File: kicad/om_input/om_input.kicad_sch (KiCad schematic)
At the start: 55 parts, among them J1 XLR3_AudioJack3_Combo_Switch, Q1 PNP, Q2 PNP, SW1 SW_DPDT_x2, SW2 SW_4PDT_x4, U1 Opamp_Quad, U2 Opamp_Quad

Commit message: improved circuit
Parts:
- removed R22, R24: 1k5, symbol Device:R_US
- added C14: 47nF, symbol Device:C
- added C15: 100pF, symbol Device:C
- added J2: Conn_01x07_Pin, symbol Connector:Conn_01x07_Pin
- C12: value 680pF -> 100nF
- C8: value 12pF -> 15pF
- R18: value 4k7 -> 470
- R21: value 1k5 -> 100
- R23: value 1k5 -> 1M
- R9: value R_US -> 2k2
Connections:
- net +48V: now also J2.1 (Pin_1)
- net +5V: now also C14.1, J2.2 (Pin_2)
- net Earth: now also J2.4 (Pin_4)
- net GND: now also C14.2, C15.1, J2.3 (Pin_3)
- net MON: now also J2.7 (Pin_7)
- net SIG+: now also J2.5 (Pin_5)
- net SIG-: now also J2.6 (Pin_6)
- net T: now also SW2.5 (B)
- net TN: no longer SW2.5 (B)
- net at SW2.9 (C): now also C13.2; no longer C13.1
- net at U2.13 (-), U2.14: now also C13.1; no longer C13.2
- net at C12.2, R23.2, U2.12 (+): now also C15.2
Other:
- note added: "(simulated approx. gain) stage 1 gain: +5db to +35db stage 2 gain: -4db to +23db stage 2 unbalanced gain: -10db to +15db inst gain: 0db mic gain: +1db to +58db line gain: -4db to +23db inst gain: -10db to +15db"
- note added: "inst and line input"
- note added: "instrument input buffer and filter ref: 1. pg 354, fig. 12.5"
- note added: "padless balanced feedback mic preamp, stage 1 ref: 1. pg. 521, fig. 17.10"
- note added: "padless balanced feedback mic preamp, stage 2 ref: 1. pg. 522, fig. 17.11"
- note added: "phantom power indicator"
- note added: "phantom power switch"
- note added: "rev log pot"
- note added: "use FET op amp ideally"
- moved on the sheet: C1, C10, C12, C13, C2, C3, C4, C5, C6, C7, C8, C9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

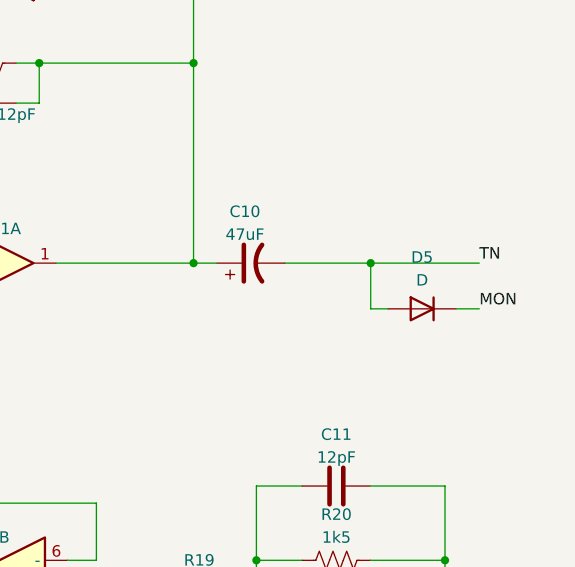
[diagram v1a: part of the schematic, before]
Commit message: removed extra mon
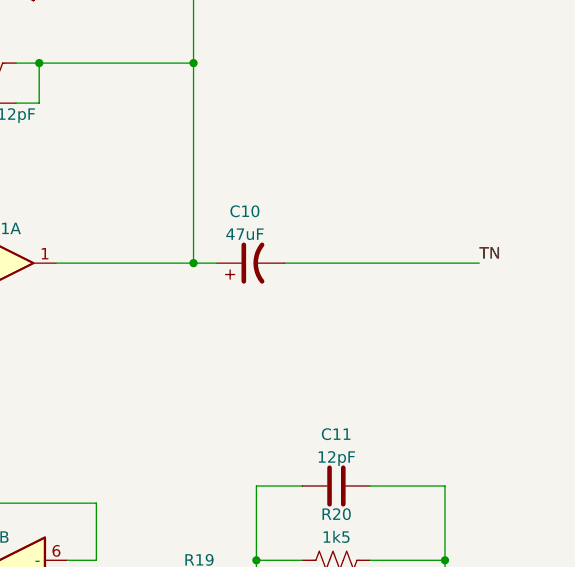
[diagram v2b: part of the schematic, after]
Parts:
- removed D5: D, symbol Device:D
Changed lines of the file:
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@@
 	)
 	(junction
-		(at 220.345 88.9)
-		(diameter 0)
-		(color 0 0 0 0)
-	)
-	(junction
 		(at 147.32 105.41)
 		(diameter 0)
@@
 	(wire
 		(pts
-			(xy 220.345 93.98) (xy 220.345 88.9)
-		)
-		(stroke
-			(width 0)
-			(type default)
-		)
-	)
-	(wire
-		(pts
 			(xy 189.865 147.32) (xy 189.865 127)
 		)
@@
 	(wire
 		(pts
-			(xy 210.82 88.9) (xy 220.345 88.9)
+			(xy 210.82 88.9) (xy 232.41 88.9)
 		)
 		(stroke
@@
 	(wire
 		(pts
-			(xy 220.345 88.9) (xy 232.41 88.9)
-		)
-		(stroke
-			(width 0)
-			(type default)
-		)
-	)
-	(wire
-		(pts
 			(xy 99.695 85.09) (xy 99.695 73.66)
 		)
@@
 	(wire
 		(pts
-			(xy 222.25 93.98) (xy 220.345 93.98)
-		)
-		(stroke
-			(width 0)
-			(type default)
-		)
-	)
-	(wire
-		(pts
-			(xy 229.87 93.98) (xy 232.41 93.98)
-		)
-		(stroke
-			(width 0)
-			(type default)
-		)
-	)
-	(wire
-		(pts
 			(xy 53.34 62.23) (xy 53.34 81.28)
 		)
@@
 		)
 	)
-	(label "MON"
-		(at 232.41 93.98 0)
-		(effects
-			(font
-				(size 1.27 1.27)
-			)
-			(justify left bottom)
-		)
-	)
 	(label "SN"
 		(at 26.67 73.66 180)
@@
 					(unit 1)
 				)
-			)
-		)
-	)
-	(symbol
-		(lib_id "Device:D")
-		(at 226.06 93.98 0)
-		(mirror y)
-		(unit 1)
-		(exclude_from_sim no)
-		(in_bom yes)
-		(on_board yes)
-		(dnp no)
-		(fields_autoplaced yes)
-		(property "Reference" "D5"
-			(at 226.06 88.265 0)
-			(effects
-				(font
-					(size 1.27 1.27)
-				)
-			)
-		)
-		(property "Value" "D"
-			(at 226.06 90.805 0)
-			(effects
-				(font
-					(size 1.27 1.27)
-				)
-			)
-		)
-		(property "Footprint" ""
-			(at 226.06 93.98 0)
-			(effects
-				(font
-					(size 1.27 1.27)
-				)
-				(hide yes)
-			)
-		)
-		(property "Datasheet" "~"
-			(at 226.06 93.98 0)
-			(effects
-				(font
-					(size 1.27 1.27)
-				)
-				(hide yes)
-			)
-		)
-		(property "Description" ""
-			(at 226.06 93.98 0)
-			(effects
-				(font
-					(size 1.27 1.27)
-				)
-			)
-		)
-		(property "Sim.Device" "D"
-			(at 226.06 93.98 0)
-			(effects
-				(font
-					(size 1.27 1.27)
-				)
-				(hide yes)
-			)
-		)
-		(property "Sim.Pins" "1=K 2=A"
-			(at 226.06 93.98 0)
-			(effects
-				(font
-					(size 1.27 1.27)
-				)
-				(hide yes)
-			)
-		)
-		(pin "1"
-		)
-		(pin "2"
-		)
-		(instances
-			(project "om_input"
-				(path "/241d8f18-f2ee-48f0-a9d7-bc33686952e8"
-					(reference "D5")
-					(unit 1)
-				)

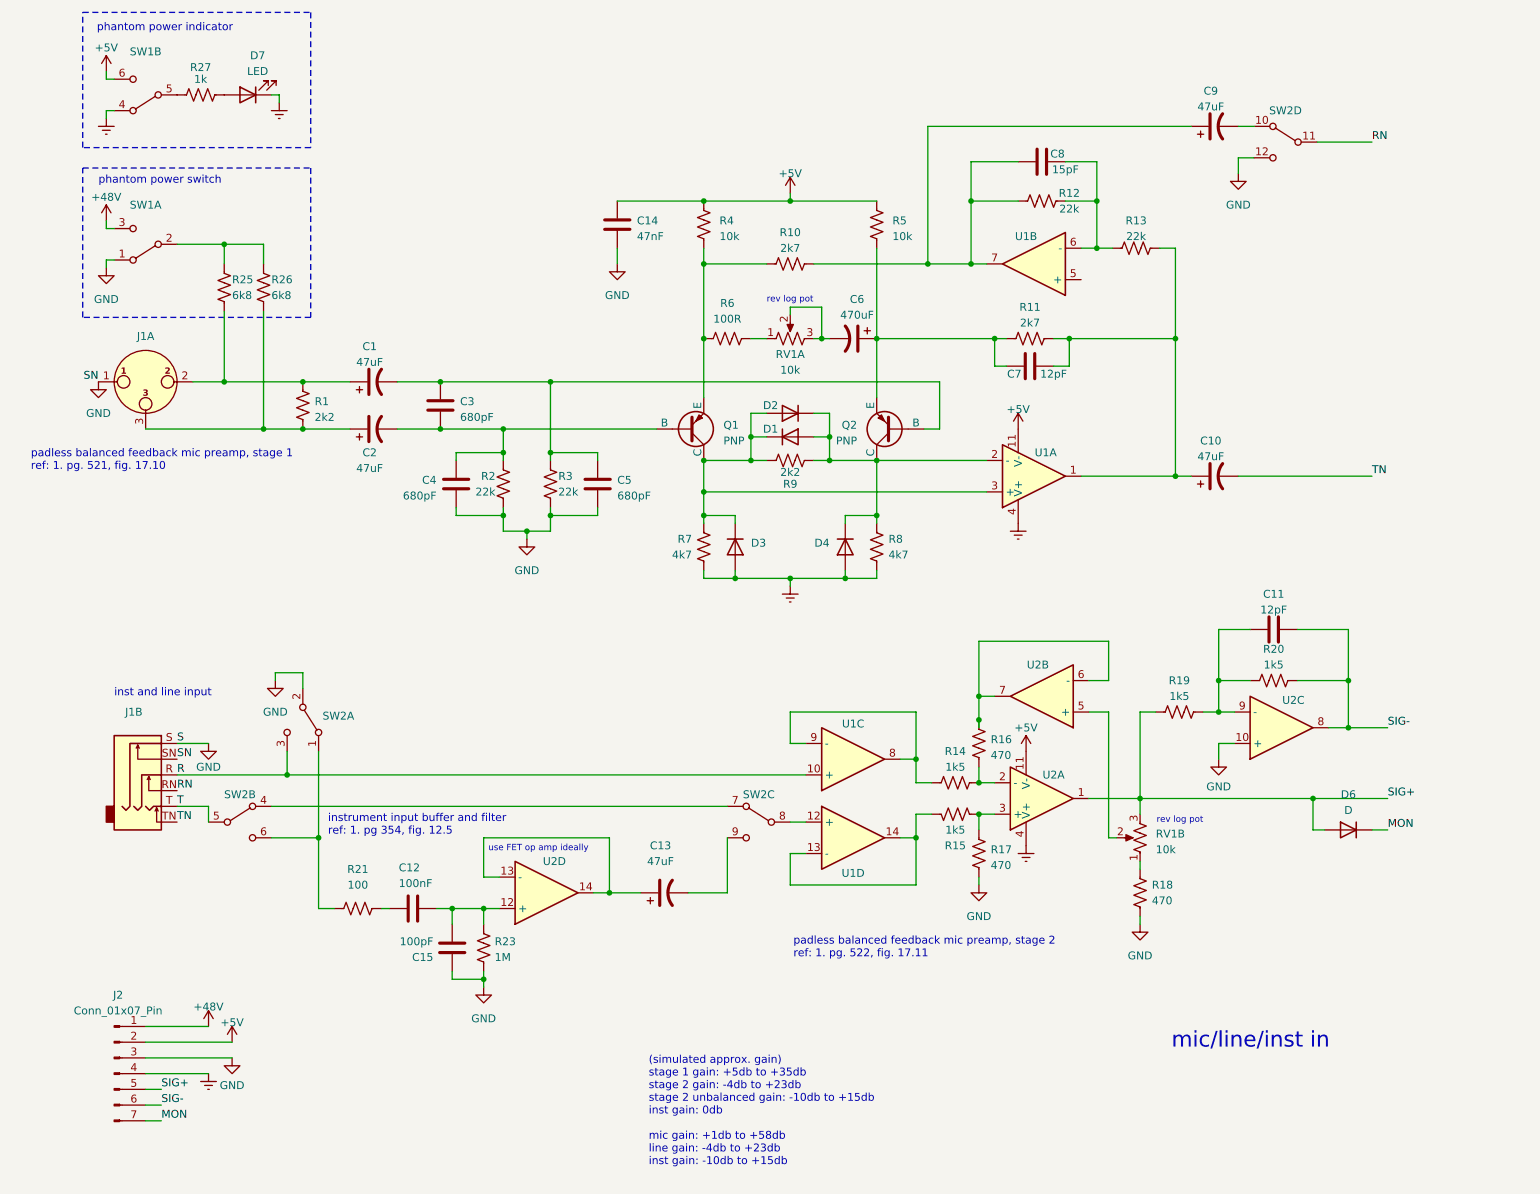
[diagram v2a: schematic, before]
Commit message: changed to 9v rails and OPA1612
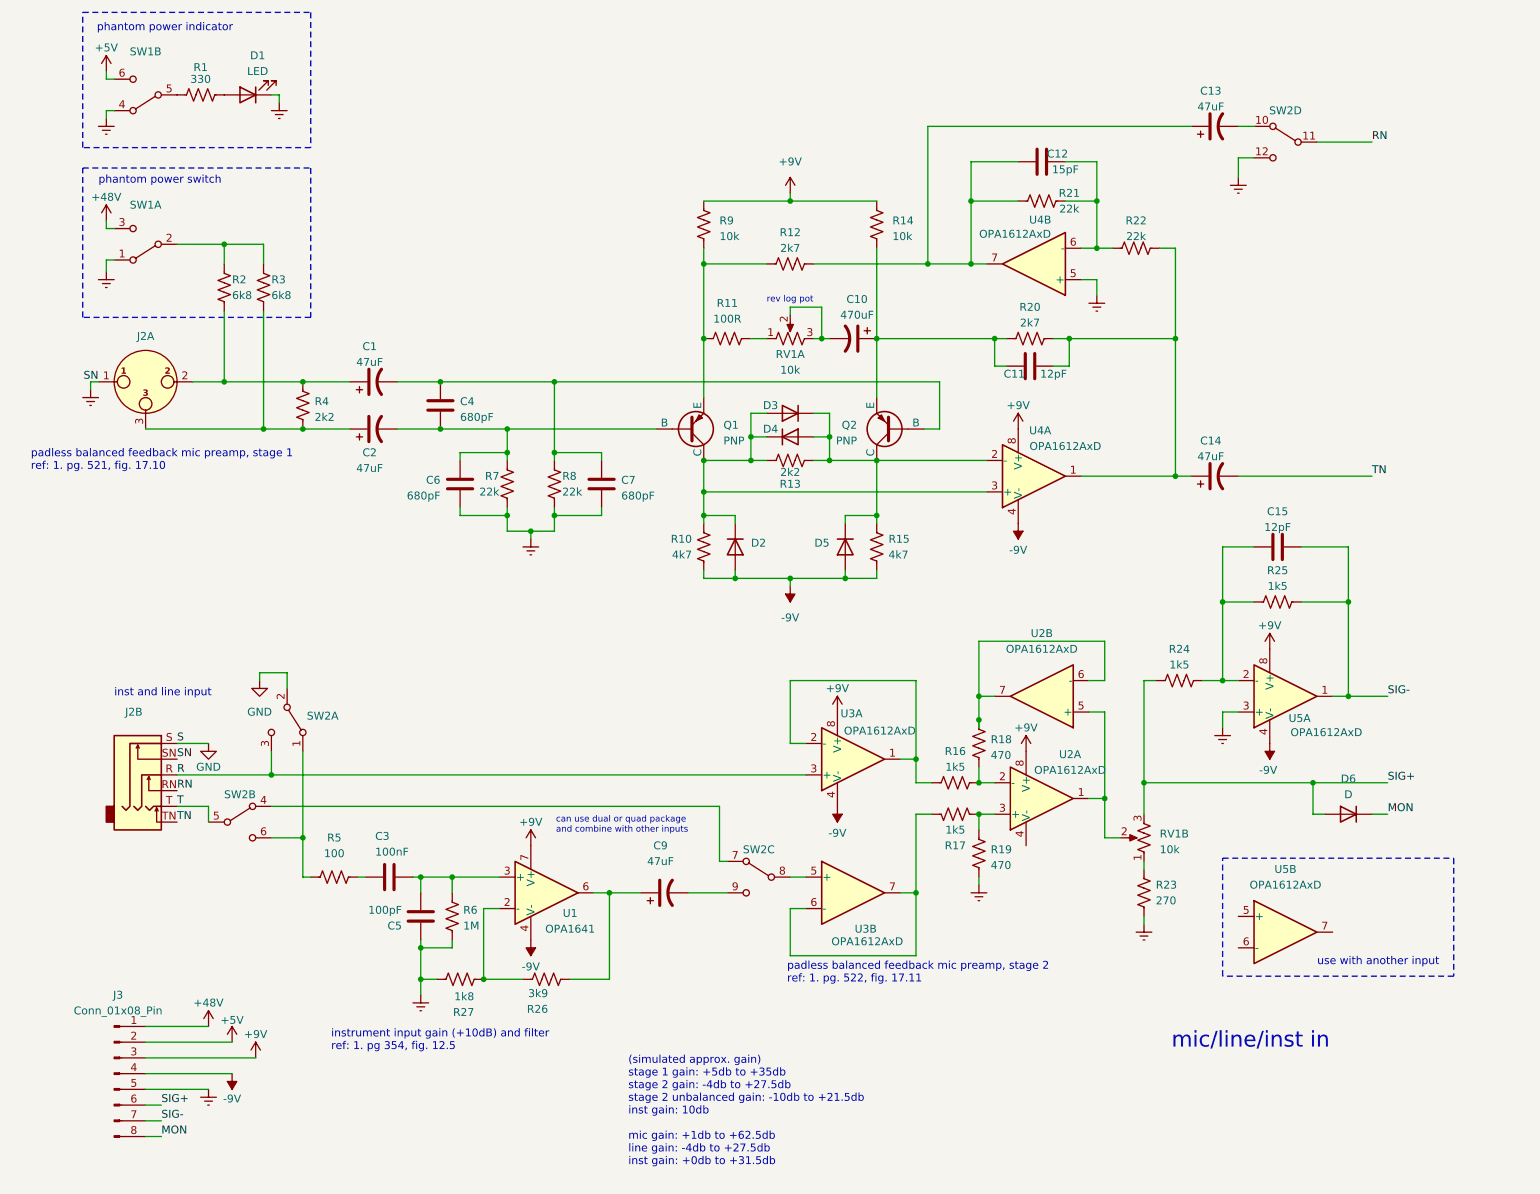
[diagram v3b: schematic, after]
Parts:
- removed C14: 47nF, symbol Device:C
- removed J2: Conn_01x07_Pin, symbol Connector:Conn_01x07_Pin
- removed U1, U2: Opamp_Quad, symbol Device:Opamp_Quad
- added J3: Conn_01x08_Pin, symbol Connector:Conn_01x08_Pin
- added R26: 3k9, symbol Device:R_US
- added R27: 1k8, symbol Device:R_US
- added U1: OPA1641, symbol Amplifier_Operational:OPA1641
- added U2, U3, U4, U5: OPA1612AxD, symbol Amplifier_Operational:OPA1612AxD
- R1: renamed from R27; value 1k -> 330
- R23: renamed from R18; value 470 -> 270
- renumbered C6 to C10, C7 to C11, C8 to C12, C9 to C13, C10 to C14, C11 to C15, C12 to C3, C3 to C4, C15 to C5, C4 to C6, C5 to C7, C13 to C9, D7 to D1, D3 to D2, D2 to D3, D1 to D4, D4 to D5, J1 to J2, R7 to R10, R6 to R11, R10 to R12, R9 to R13, R5 to R14, R8 to R15, R14 to R16, R15 to R17, R16 to R18, R17 to R19, R25 to R2, R11 to R20, R12 to R21, R13 to R22, R19 to R24, R20 to R25, R26 to R3, R1 to R4, R21 to R5, R23 to R6, R2 to R7, R3 to R8, R4 to R9
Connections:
- net +48V: now also J3.1 (Pin_1)
- net +5V: now also J3.2 (Pin_2); no longer R14.1, R9.1
- net Earth: now also C5.1, C6.2, C7.2, J2.1, J2.SN, R19.2, R23.2, R6.1, R7.2, R8.2, SW1.1 (A), SW2.12 (C), J3.5 (Pin_5), R27.2, U4.5 (+), U5.3 (+); no longer D2.2 (A), D5.2 (A), R10.2, R15.2
- net GND: no longer C5.1, C6.2, C7.2, J2.1, J2.SN, R19.2, R23.2, R6.1, R7.2, R8.2, SW1.1 (A), SW2.12 (C)
- net MON: now also J3.8 (Pin_8)
- net R: now also U3.3 (+)
- net SIG+: now also J3.6 (Pin_6)
- net SIG-: now also J3.7 (Pin_7), U5.1
- net at R17.1: now also U3.6 (-), U3.7
- net at R17.2, R19.1: now also U2.3 (+)
- net at D3.1 (K), D4.2 (A), D5.1 (K)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: now also U4.2 (-)
- net at R18.1: now also U2.6 (-), U2.7
- net at R16.2, R18.2: now also U2.2 (-)
- net at SW2.8 (B): now also U3.5 (+)
- net at C15.1, R24.2, R25.1: now also U5.2 (-)
- net at D2.1 (K), D3.2 (A), D4.1 (K)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: now also U4.3 (+)
- net at C9.1: now also R26.1, U1.6
- net at C12.1, C13.1, R12.2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: now also U4.7
- net at C12.2, R21.2, R22.1: now also U4.6 (-)
- net at R16.1: now also U3.1, U3.2 (-)
- net at C11.2, C14.1, R20.2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: now also U4.1
- net at RV1.2: now also U2.1, U2.5 (+)
- net at C3.2, C5.2, R6.2: now also U1.3 (+)
- new net: R26.2, R27.1, U1.2 (-)
- new net +9V: J3.3 (Pin_3), R14.1, R9.1, U1.7 (V+), U2.8 (V+), U3.8 (V+), U4.8 (V+), U5.8 (V+)
- new net -9V: D2.2 (A), D5.2 (A), J3.4 (Pin_4), R10.2, R15.2, U1.4 (V-), U2.4 (V-), U4.4 (V-), U5.4 (V-)
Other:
- note added: "(simulated approx. gain) stage 1 gain: +5db to +35db stage 2 gain: -4db to +27.5db stage 2 unbalanced gain: -10db to +21.5db inst gain: 10db mic gain: +1db to +62.5db line gain: -4db to +27.5db inst gain: +0db to +31.5db"
- note added: "can use dual or quad package and combine with other inputs"
- note added: "instrument input gain (+10dB) and filter ref: 1. pg 354, fig. 12.5"
- note added: "use with another input"
- note removed: "(simulated approx. gain) stage 1 gain: +5db to +35db stage 2 gain: -4db to +23db stage 2 unbalanced gain: -10db to +15db inst gain: 0db mic gain: +1db to +58db line gain: -4db to +23db inst gain: -10db to +15db"
- note removed: "instrument input buffer and filter ref: 1. pg 354, fig. 12.5"
- note removed: "use FET op amp ideally"
- moved on the sheet: C15, C3, C5, C6, C7, D6, R23, R24, R25, R5, R6, R7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

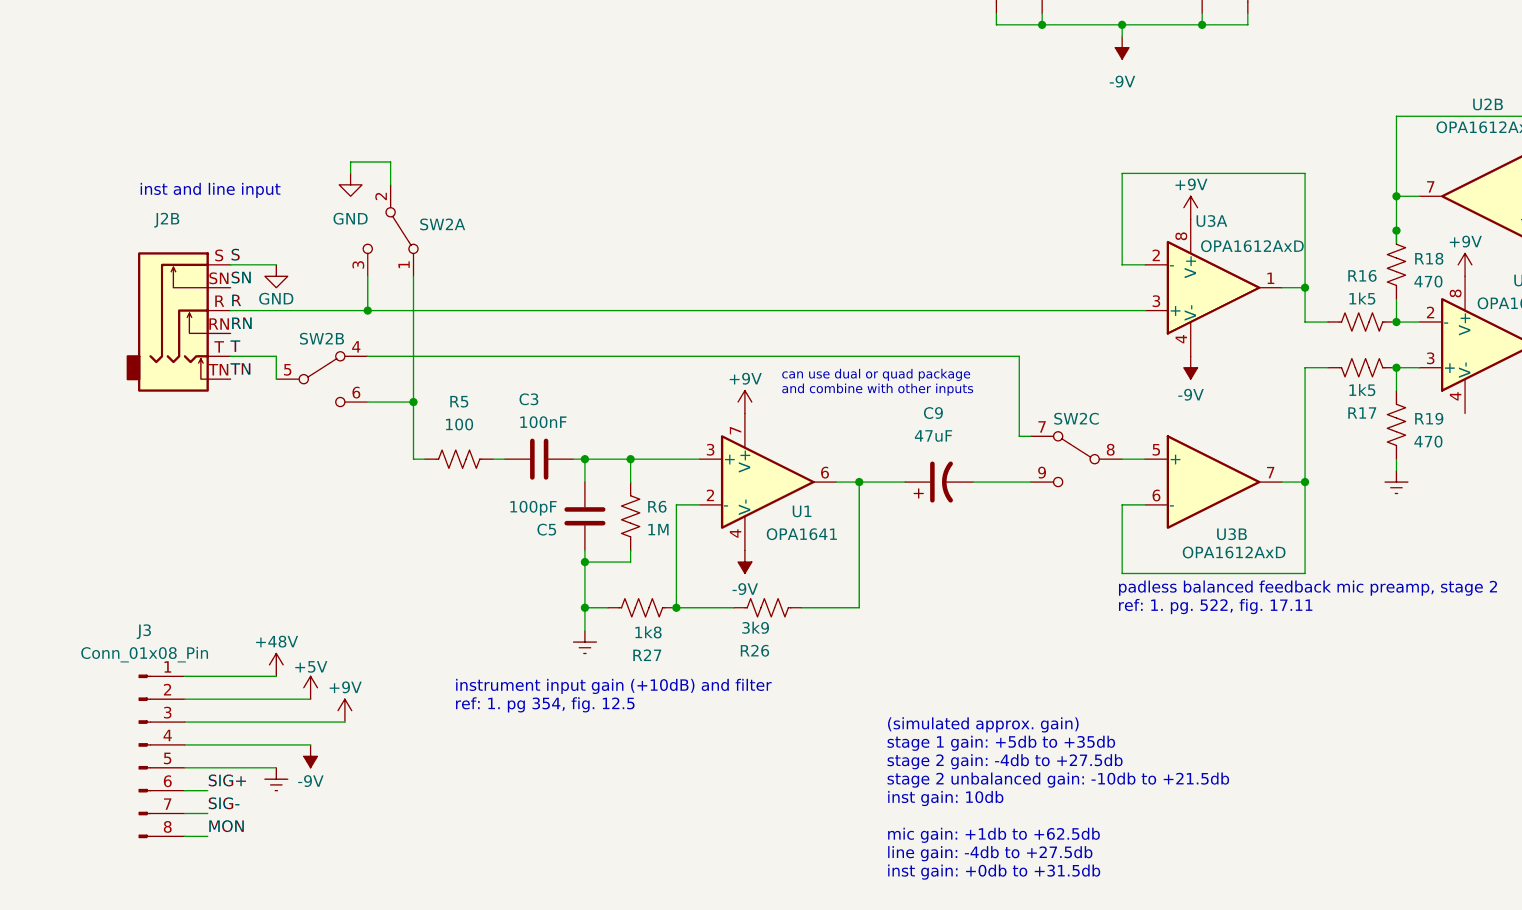
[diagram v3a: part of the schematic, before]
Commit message: fixed ground symbols and spacing
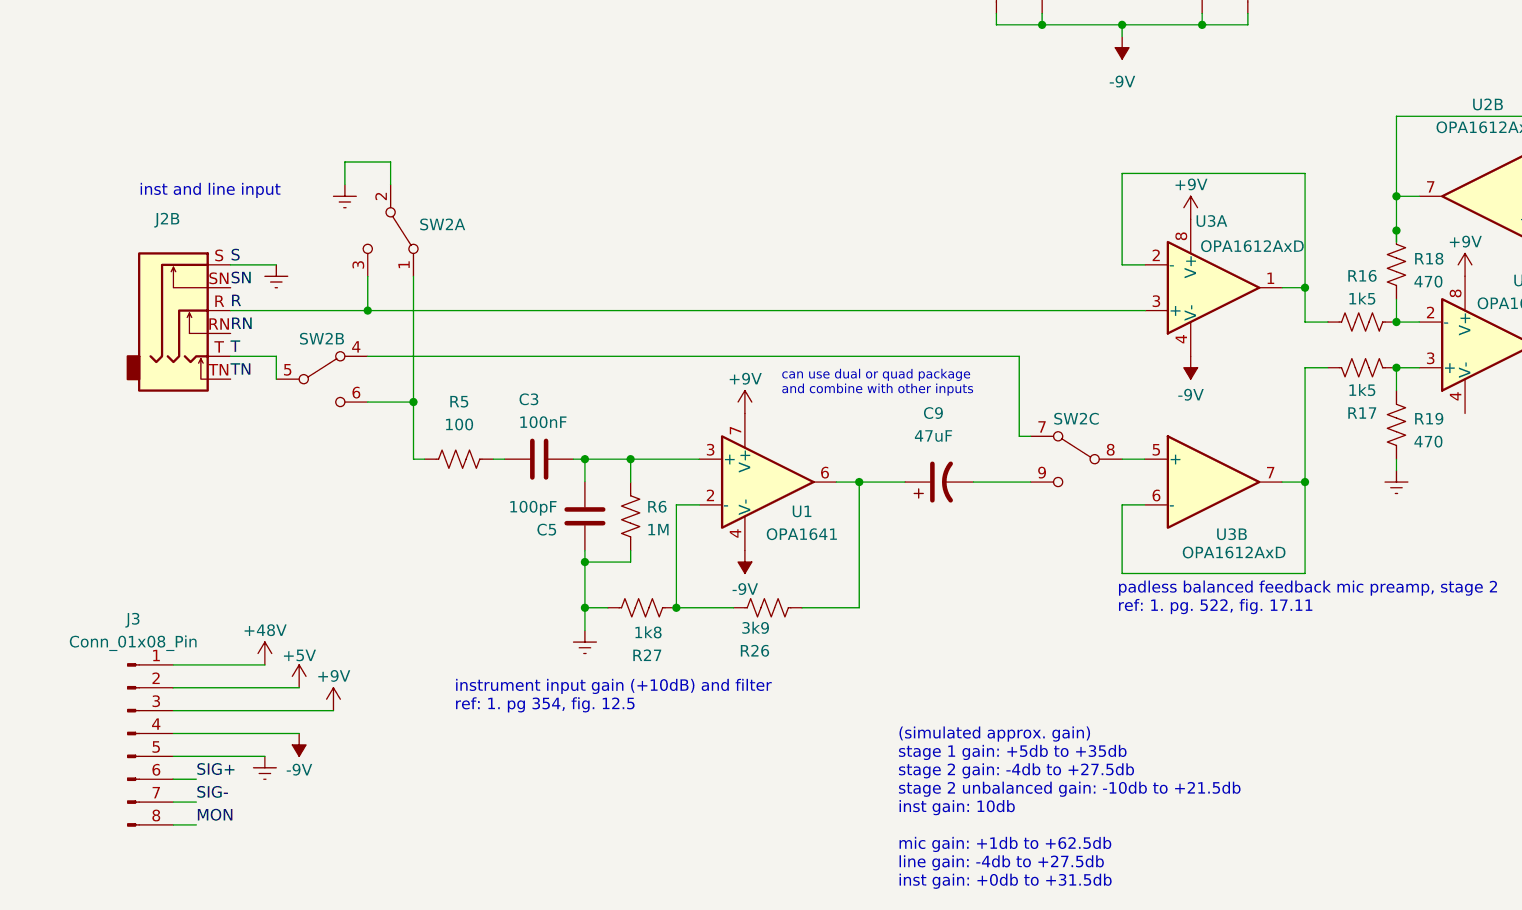
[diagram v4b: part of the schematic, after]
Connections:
- net GND is gone; now on net Earth: J2.S, SW2.2 (B)
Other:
- moved on the sheet: J3
